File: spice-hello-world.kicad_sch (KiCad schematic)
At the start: 4 parts

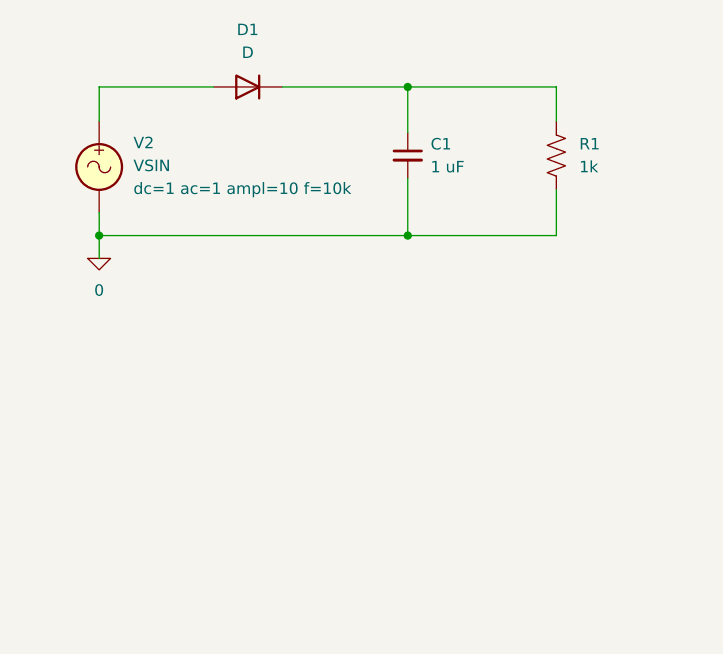
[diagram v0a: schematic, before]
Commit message: feat: add specialized circuit schematics
- Updated main spice-hello-world schematic with improved layout
- Added dedicated half-wave rectifier circuit schematic
- Added TTL NAND gate circuit schematic for digital simulation
- Removed unused untitled schematic
- Updated project configuration and workbook settings
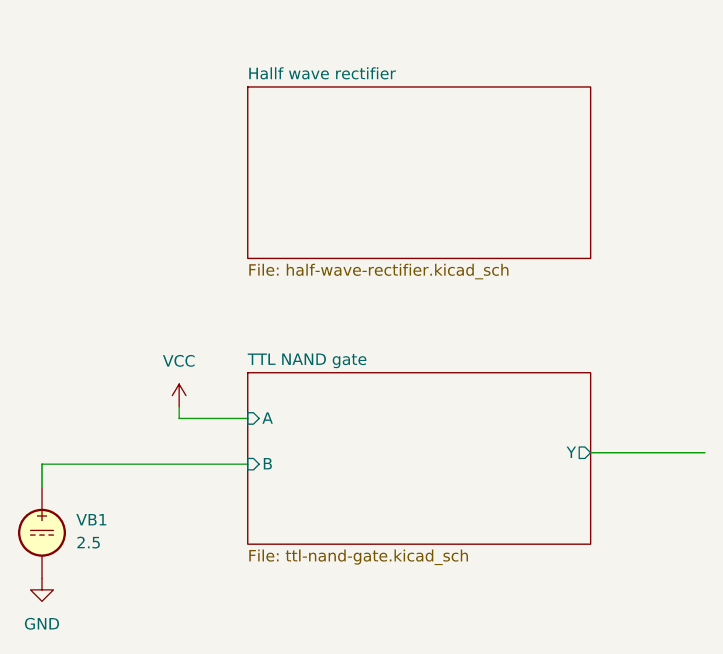
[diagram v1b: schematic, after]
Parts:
- removed C1: 1 uF, symbol Device:C_Small
- removed D1: D, symbol Simulation_SPICE:D
- removed R1: 1k, symbol Device:R_US
- removed V2: VSIN, symbol Simulation_SPICE:VSIN
- added VB1: 2.5, symbol Simulation_SPICE:VDC
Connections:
- new net GND: VB1.2
- new net TTL NAND gate/B: VB1.1
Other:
- added sheet Hallf wave rectifier (half-wave-rectifier.kicad_sch)
- added sheet TTL NAND gate (ttl-nand-gate.kicad_sch)
